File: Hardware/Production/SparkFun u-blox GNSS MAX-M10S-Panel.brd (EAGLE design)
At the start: 38.1 x 30.5 mm, 90 parts, among them J1 USB-to-Serial, J2 Qwiic RA, J3 PTH, J4 Qwiic RA, U1 MAX-M10S

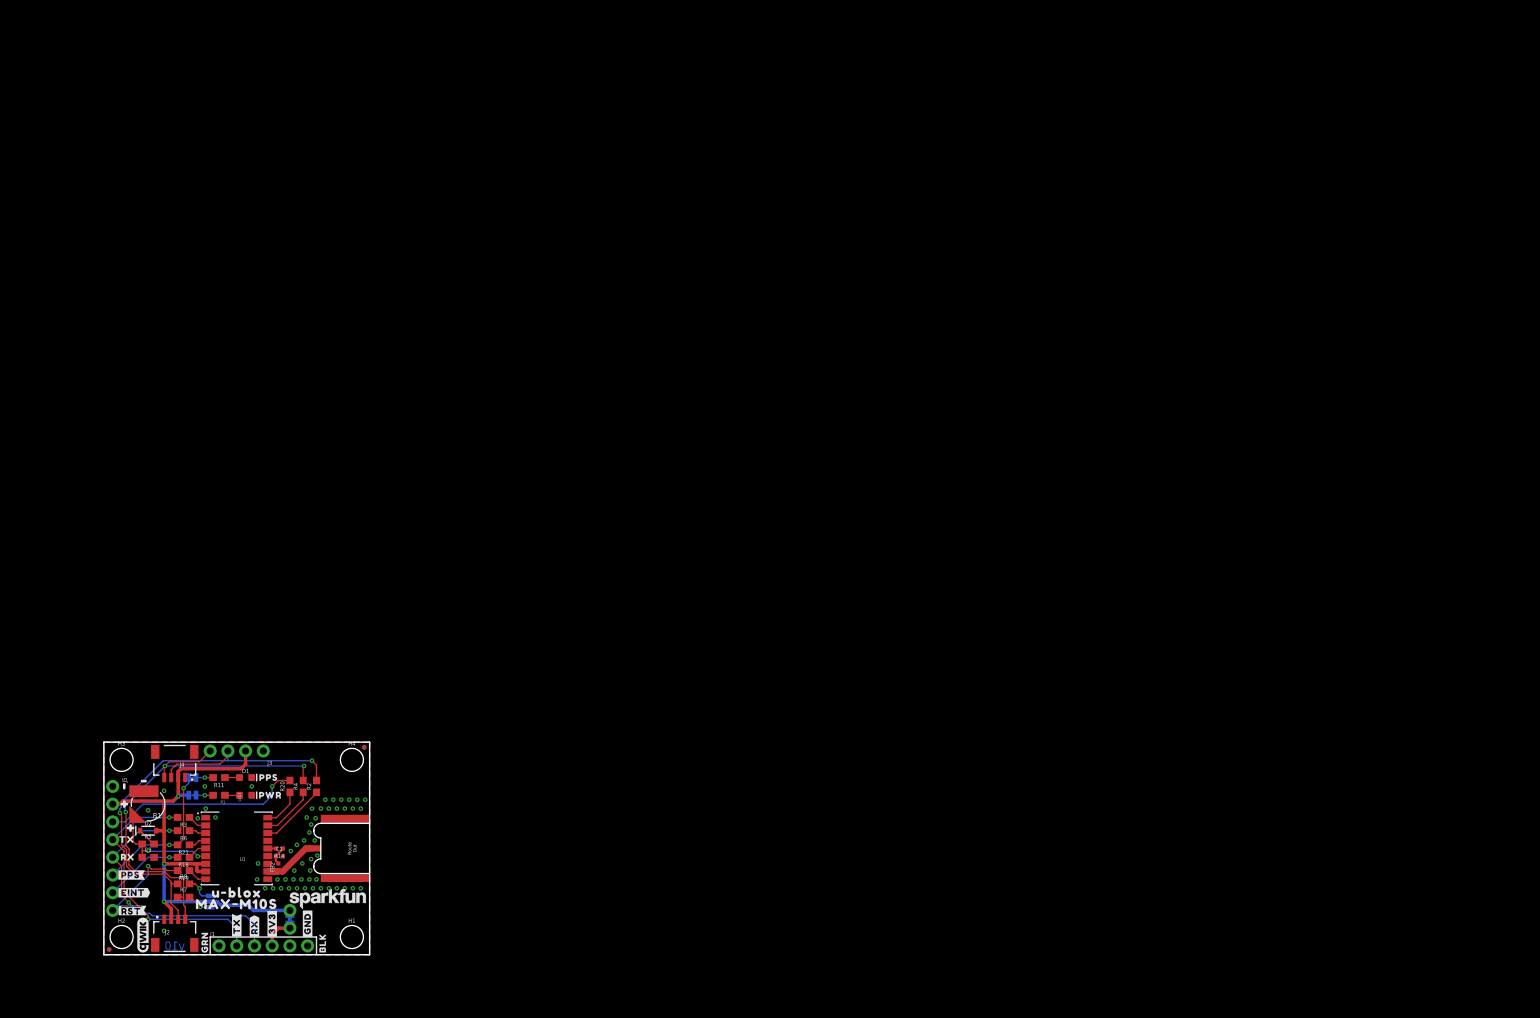
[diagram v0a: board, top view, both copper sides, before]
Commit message: Changing RF path to 0402. Adding GND vias on both RF trace sides. Adding panel.
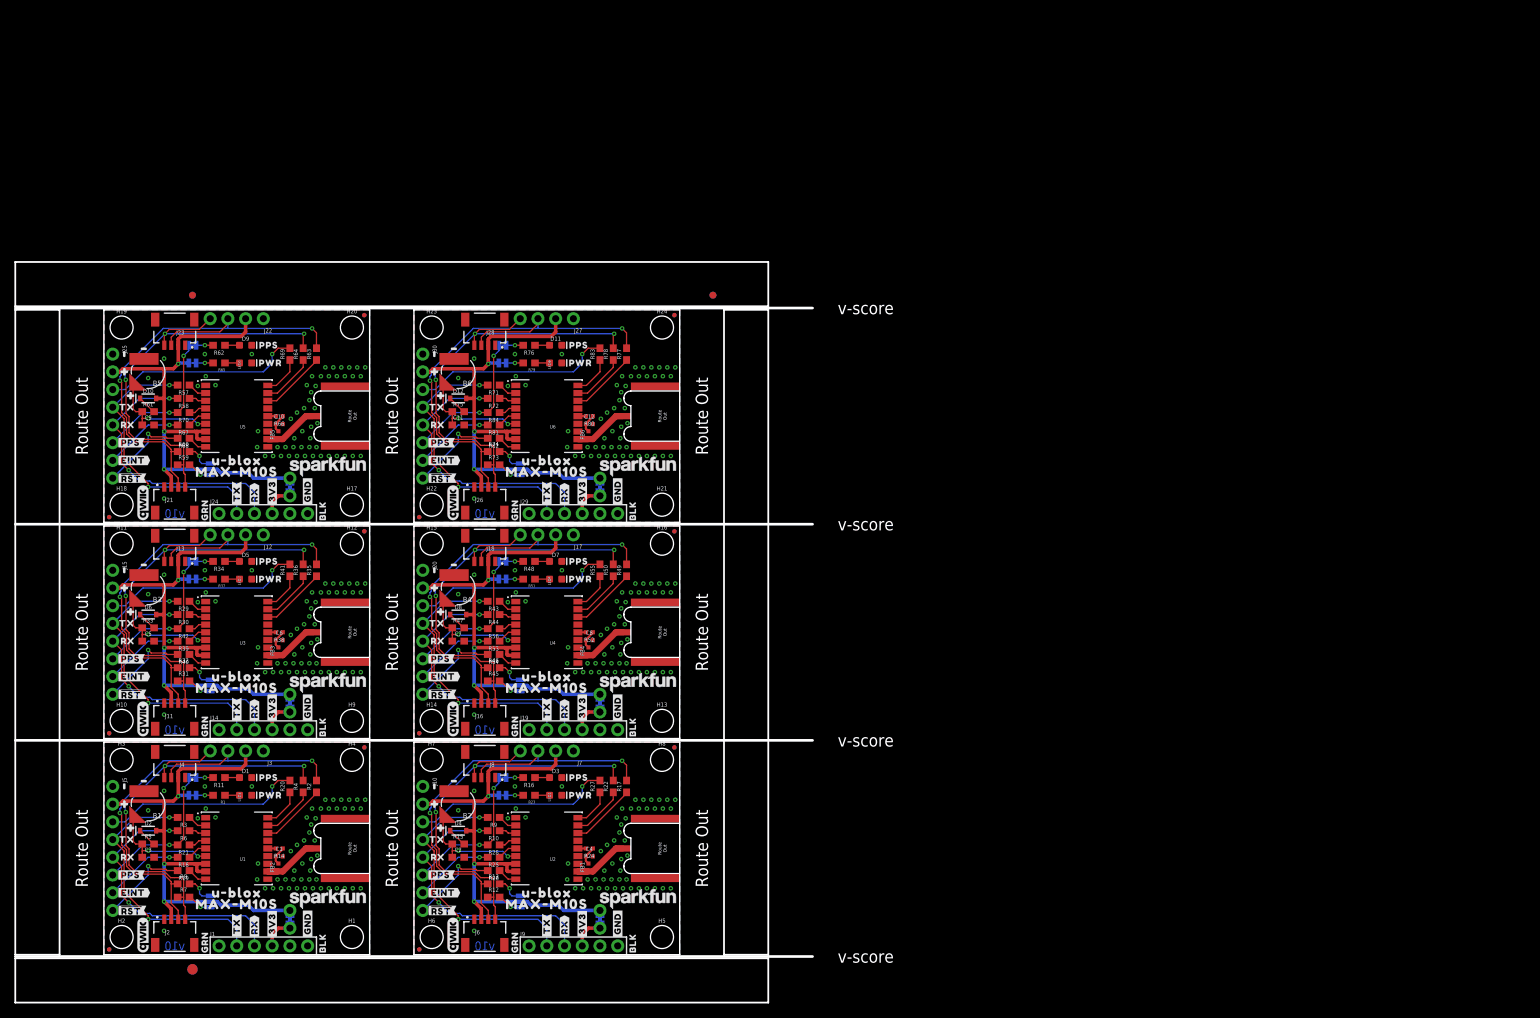
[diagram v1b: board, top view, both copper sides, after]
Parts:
- removed FRAME1: FRAME-LETTER, SparkFun-Aesthetics:CREATIVE_COMMONS
- added B2, B3, B4, B5, B6: 6.8MM_COIN_CELL, SparkFun-Batteries:ML414H_IV01E
- added C10, C12, C4, C6, C8: 47PF-0402_TIGHT-25V-5%-X7R, SparkFun-Capacitors:0402-TIGHT
- added C11, C2, C5, C7, C9: 1.0uF, SparkFun-Capacitors:0603
- added D10, D12, D4, D6, D8: 0.5A/40V/420mV, SparkFun-DiscreteSemi:SOD-323
- added D11, D3, D5, D7, D9: Yellow, SparkFun-LED:LED-0603
- added E$1, E$2, E$3, E$4: (no value), SparkFun-Aesthetics:FIDUCIAL-1X2
- added E$5, E$6: (no value), SparkFun-Retired:FIDUCIAL-1.5X3
- added E2, E3, E4, E5, E6: (no value), SparkFun-RF:SMA-EDGE-SMD
- added FB1, FB3, FB4, FB5, FB6: 2.66Ω, SparkFun-Coils:0402-TIGHT
- added FD10, FD11, FD12, FD13, FD14, FD15, FD16, FD17, FD18, FD19, FD20, FD21, FD22, FD23, FD24, FD5, FD6, FD7, FD8, FD9: FIDUCIALUFIDUCIAL, SparkFun-Aesthetics:FIDUCIAL-MICRO
- added H10, H11, H12, H13, H14, H15, H16, H17, H18, H19, H20, H21, H22, H23, H24, H5, H6, H7, H8, H9: STAND-OFF, SparkFun-Hardware:STAND-OFF
- added J10, J15, J20, J25, J30: (no value), SparkFun-Connectors:1X08_NO_SILK
- added J11, J13, J16, J18, J21, J23, J26, J28, J6, J8: Qwiic RA, SparkFun-Connectors:JST04_1MM_RA
- added J12, J17, J22, J27, J7: PTH, SparkX:1X04_NO_SILK
- added J14, J19, J24, J29, J9: USB-to-Serial, SparkFun-Connectors:1X06_NO_SILK
- added JP1, JP2, JP3, JP4, JP6: (no value), SparkFun-Jumpers:SMT-JUMPER_3_NO_SILK
- added LED1, LED3, LED4, LED5, LED6: RED, SparkFun-LED:LED-0603
- added LOGO10, LOGO14, LOGO18, LOGO22, LOGO6: SFE_LOGO_NAME_FLAME.1_INCH, SparkFun-Aesthetics:SFE_LOGO_NAME_FLAME_.1
- added LOGO11, LOGO15, LOGO19, LOGO23, LOGO7: QWIIC_LOGO_5MM, SparkFun-Aesthetics:QWIIC_5MM
- added LOGO12, LOGO16, LOGO20, LOGO24, LOGO8: SFE_LOGO_NAME.1_INCH, SparkFun-Aesthetics:SFE_LOGO_NAME_.1
- added LOGO13, LOGO17, LOGO21, LOGO5, LOGO9: OSHW-LOGOMINI, SparkFun-Aesthetics:OSHW-LOGO-MINI
- added MEAS1, MEAS2, MEAS3, MEAS4, MEAS5: (no value), SparkFun-Jumpers:COMBO-JUMPER_2_NC_TRACE
- added PPS_LED1, PPS_LED2, PPS_LED3, PPS_LED4, PPS_LED5, PWR1, PWR2, PWR3, PWR4, PWR5: (no value), SparkFun-Jumpers:SMT-JUMPER_2_NC_TRACE_SILK
- added R10, R17, R22, R25, R26, R27, R28, R29, R30, R35, R36, R39, R40, R41, R42, R43, R44, R49, R50, R53, R54, R55, R56, R57, R58, R63, R64, R67, R68, R69, R70, R71, R72, R77, R78, R81, R82, R83, R84, R9: 33, SparkFun-Resistors:0603
- added R12, R13, R31, R32, R45, R46, R59, R60, R73, R74: 2.2k, SparkFun-Resistors:0603
- added R15, R33, R47, R61, R75: 3.3k, SparkFun-Resistors:0603
- added R16, R23, R34, R37, R48, R51, R62, R65, R76, R79: 1k, SparkFun-Resistors:0603
- added R24, R38, R52, R66, R80: 33OHM-0402T-1/10W-1%, SparkFun-Resistors:0402-TIGHT
- added U$100, U$144, U$188, U$232, U$56: (no value), output:##SAFE##0
- added U$101, U$126, U$145, U$170, U$189, U$214, U$233, U$258, U$57, U$82: (no value), output:#PPS#1
- added U$102, U$146, U$190, U$234, U$58: (no value), output:#RX#1
- added U$103, U$147, U$191, U$235, U$59: (no value), output:#TX#0
- added U$104, U$107, U$148, U$151, U$192, U$195, U$236, U$239, U$60, U$63: (no value), output:MAX#M10S1
- added U$105, U$106, U$149, U$150, U$193, U$194, U$237, U$238, U$61, U$62: (no value), output:U#BLOX0
- added U$108, U$152, U$196, U$240, U$64: (no value), output:SMA2
- added U$109, U$140, U$153, U$184, U$197, U$228, U$241, U$52, U$65, U$96: (no value), output:#TX#3
- added U$110, U$139, U$154, U$183, U$198, U$227, U$242, U$51, U$66, U$95: (no value), output:#RX#2
- added U$111, U$118, U$133, U$141, U$155, U$162, U$177, U$185, U$199, U$206, U$221, U$229, U$243, U$250, U$53, U$67, U$74, U$89, U$97: (no value), output:#3V3#4
- added U$112, U$119, U$134, U$142, U$156, U$163, U$17, U$178, U$186, U$200, U$207, U$222, U$230, U$244, U$251, U$54, U$68, U$75, U$90, U$98: (no value), output:#GND#5
- added U$113, U$135, U$157, U$179, U$201, U$223, U$245, U$47, U$69, U$91: (no value), output:BLK0
- added U$114, U$136, U$158, U$180, U$202, U$224, U$246, U$48, U$70, U$92: (no value), output:GRN1
- added U$115, U$159, U$203, U$247, U$71: (no value), output:#I�C#0
- added U$116, U$160, U$204, U$248, U$72: (no value), output:#SCL#1
- added U$117, U$161, U$205, U$249, U$73: (no value), output:#SDA#0
- added U$120, U$164, U$208, U$252, U$76: (no value), output:#PPS#0
- added U$121, U$165, U$209, U$253, U$77: (no value), output:#PWR#0
- added U$122, U$129, U$166, U$173, U$210, U$217, U$254, U$261, U$78, U$85: (no value), output:#0
- added U$123, U$130, U$167, U$174, U$211, U$218, U$255, U$262, U$79, U$86: (no value), output:#1
- added U$124, U$168, U$212, U$256, U$80: (no value), output:##RST##0
- added U$125, U$169, U$213, U$257, U$81: (no value), output:#EINT#0
- added U$127, U$171, U$215, U$259, U$83: (no value), output:RX2
- added U$128, U$172, U$216, U$260, U$84: (no value), output:TX3
- added U$131, U$175, U$219, U$263, U$87: (no value), output:#MEAS#0
- added U$132, U$176, U$220, U$264, U$88: (no value), output:#EINT_#0
- added U$137, U$181, U$225, U$49, U$93: (no value), output:PPS7
- added U$138, U$182, U$226, U$50, U$94: (no value), output:PWR6
- added U$143, U$187, U$231, U$55, U$99: (no value), output:##RST##2
- added U2, U3, U4, U5, U6: MAX-M10S, GNSS-MAX:MAX-M10S
- U$2: value SPECIAL_INSTRUCTIONS-ORDERING -> (none); device SparkFun-Aesthetics:ORDERING_INSTRUCTIONS -> output:#3V3#4
- moved U$2 51.5 mm to (68.6, 4.45), turned to 90 degrees
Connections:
- new net !RESET1: J10.8, R26.2
- new net !RESET2: J15.8, R40.2
- new net !RESET3: J20.8, R54.2
- new net !RESET4: J25.8, R68.2
- new net !RESET5: J30.8, R82.2
- new net !SAFE1: J10.3, R27.2
- new net !SAFE2: J15.3, R41.2
- new net !SAFE3: J20.3, R55.2
- new net !SAFE4: J25.3, R69.2
- new net !SAFE5: J30.3, R83.2
- new net 3.3V1: D4.A, J10.2, J6.2, J7.2, J8.2, JP1.2, MEAS1.2, MEAS1.4, PWR1.2, U2.7, U2.8
- new net 3.3V2: D6.A, J11.2, J12.2, J13.2, J15.2, JP2.2, MEAS2.2, MEAS2.4, PWR2.2, U3.7, U3.8
- new net 3.3V3: D8.A, J16.2, J17.2, J18.2, J20.2, JP3.2, MEAS3.2, MEAS3.4, PWR3.2, U4.7, U4.8
- new net 3.3V4: D10.A, J21.2, J22.2, J23.2, J25.2, JP4.2, MEAS4.2, MEAS4.4, PWR4.2, U5.7, U5.8
- new net 3.3V5: D12.A, J26.2, J27.2, J28.2, J30.2, JP6.2, MEAS5.2, MEAS5.4, PWR5.2, U6.7, U6.8
- new net ANT_VCC1: C4.1, FB1.2, R24.1
- new net ANT_VCC2: C6.1, FB3.2, R38.1
- new net ANT_VCC3: C8.1, FB4.2, R52.1
- new net ANT_VCC4: C10.1, FB5.2, R66.1
- new net ANT_VCC5: C12.1, FB6.2, R80.1
- new net BACKUP1: B2.+, C2.1, R15.1, U2.6
- new net BACKUP2: B3.+, C5.1, R33.1, U3.6
- new net BACKUP3: B4.+, C7.1, R47.1, U4.6
- new net BACKUP4: B5.+, C9.1, R61.1, U5.6
- new net BACKUP5: B6.+, C11.1, R75.1, U6.6
- new net EXTINT_LV1: R25.1, U2.5
- new net EXTINT_LV2: R39.1, U3.5
- new net EXTINT_LV3: R53.1, U4.5
- new net EXTINT_LV4: R67.1, U5.5
- new net EXTINT_LV5: R81.1, U6.5
- new net GND1: B2.-, C2.2, C4.2, D3.C, E2.GND@0, E2.GND@1, J10.1, J6.1, J7.1, J8.1, J9.6, LED1.C, U2.1, U2.10, U2.12
- new net GND2: B3.-, C5.2, C6.2, D5.C, E3.GND@0, E3.GND@1, J11.1, J12.1, J13.1, J14.6, J15.1, LED3.C, U3.1, U3.10, U3.12
- new net GND3: B4.-, C7.2, C8.2, D7.C, E4.GND@0, E4.GND@1, J16.1, J17.1, J18.1, J19.6, J20.1, LED4.C, U4.1, U4.10, U4.12
- new net GND4: B5.-, C10.2, C9.2, D9.C, E5.GND@0, E5.GND@1, J21.1, J22.1, J23.1, J24.6, J25.1, LED5.C, U5.1, U5.10, U5.12
- new net GND5: B6.-, C11.2, C12.2, D11.C, E6.GND@0, E6.GND@1, J26.1, J27.1, J28.1, J29.6, J30.1, LED6.C, U6.1, U6.10, U6.12
- new net GPS_RF1: E2.SIG, FB1.1, U2.11
- new net GPS_RF2: E3.SIG, FB3.1, U3.11
- new net GPS_RF3: E4.SIG, FB4.1, U4.11
- new net GPS_RF4: E5.SIG, FB5.1, U5.11
- new net GPS_RF5: E6.SIG, FB6.1, U6.11
- new net INT1: J10.7, R25.2
- new net INT2: J15.7, R39.2
- new net INT3: J20.7, R53.2
- new net INT4: J25.7, R67.2
- new net INT5: J30.7, R81.2
- new net N$11: PPS_LED1.1, R16.2
- new net N$12: D4.C, R15.2
- new net N$13: LED1.A, R23.1
- new net N$14: PWR1.1, R23.2
- new net N$15: J9.4, MEAS1.1, MEAS1.3
- new net N$16: JP2.1, R32.2
- new net N$18: JP2.3, R31.2
- new net N$19: D5.A, R34.1
- new net N$20: PPS_LED2.1, R34.2
- new net N$21: D6.C, R33.2
- new net N$22: LED3.A, R37.1
- new net N$23: PWR2.1, R37.2
- new net N$24: J14.4, MEAS2.1, MEAS2.3
- new net N$25: JP3.1, R46.2
- new net N$26: JP3.3, R45.2
- new net N$27: D7.A, R48.1
- new net N$28: PPS_LED3.1, R48.2
- new net N$29: D8.C, R47.2
- new net N$3: JP1.1, R13.2
- new net N$30: LED4.A, R51.1
- new net N$31: PWR3.1, R51.2
- new net N$32: J19.4, MEAS3.1, MEAS3.3
- new net N$33: JP4.1, R60.2
- new net N$34: JP4.3, R59.2
- new net N$35: D9.A, R62.1
- new net N$36: PPS_LED4.1, R62.2
- new net N$37: D10.C, R61.2
- new net N$38: LED5.A, R65.1
- new net N$39: PWR4.1, R65.2
- new net N$40: J24.4, MEAS4.1, MEAS4.3
- new net N$41: JP6.1, R74.2
- new net N$42: JP6.3, R73.2
- new net N$43: D11.A, R76.1
- new net N$44: PPS_LED5.1, R76.2
- new net N$45: D12.C, R75.2
- new net N$46: LED6.A, R79.1
- new net N$47: PWR5.1, R79.2
- new net N$48: J29.4, MEAS5.1, MEAS5.3
- new net N$7: JP1.3, R12.2
- new net N$9: D3.A, R16.1
- new net PPS1: J10.6, PPS_LED1.2, R28.2
- new net PPS2: J15.6, PPS_LED2.2, R42.2
- new net PPS3: J20.6, PPS_LED3.2, R56.2
- new net PPS4: J25.6, PPS_LED4.2, R70.2
- new net PPS5: J30.6, PPS_LED5.2, R84.2
- new net PPS_LV1: R28.1, U2.4
- new net PPS_LV2: R42.1, U3.4
- new net PPS_LV3: R56.1, U4.4
- new net PPS_LV4: R70.1, U5.4
- new net PPS_LV5: R84.1, U6.4
- new net RST_LV1: R26.1, U2.9
- new net RST_LV2: R40.1, U3.9
- new net RST_LV3: R54.1, U4.9
- new net RST_LV4: R68.1, U5.9
- new net RST_LV5: R82.1, U6.9
- new net RXI1: J10.5, J9.3, R10.2
- new net RXI2: J14.3, J15.5, R30.2
- new net RXI3: J19.3, J20.5, R44.2
- new net RXI4: J24.3, J25.5, R58.2
- new net RXI5: J29.3, J30.5, R72.2
- new net RXLV1: R10.1, U2.3
- new net RXLV2: R30.1, U3.3
- new net RXLV3: R44.1, U4.3
- new net RXLV4: R58.1, U5.3
- new net RXLV5: R72.1, U6.3
- new net SAFE_LV1: R27.1, U2.18
- new net SAFE_LV2: R41.1, U3.18
- new net SAFE_LV3: R55.1, U4.18
- new net SAFE_LV4: R69.1, U5.18
- new net SAFE_LV5: R83.1, U6.18
- new net SCL1: J6.4, J7.4, J8.4, R12.1, R22.2
- new net SCL2: J11.4, J12.4, J13.4, R31.1, R36.2
- new net SCL3: J16.4, J17.4, J18.4, R45.1, R50.2
- new net SCL4: J21.4, J22.4, J23.4, R59.1, R64.2
- new net SCL5: J26.4, J27.4, J28.4, R73.1, R78.2
- new net SCL_LV1: R22.1, U2.17
- new net SCL_LV2: R36.1, U3.17
- new net SCL_LV3: R50.1, U4.17
- new net SCL_LV4: R64.1, U5.17
- new net SCL_LV5: R78.1, U6.17
- new net SDA1: J6.3, J7.3, J8.3, R13.1, R17.2
- new net SDA2: J11.3, J12.3, J13.3, R32.1, R35.2
- new net SDA3: J16.3, J17.3, J18.3, R46.1, R49.2
- new net SDA4: J21.3, J22.3, J23.3, R60.1, R63.2
- new net SDA5: J26.3, J27.3, J28.3, R74.1, R77.2
- new net SDA_LV1: R17.1, U2.16
- new net SDA_LV2: R35.1, U3.16
- new net SDA_LV3: R49.1, U4.16
- new net SDA_LV4: R63.1, U5.16
- new net SDA_LV5: R77.1, U6.16
- new net TXLV1: R9.1, U2.2
- new net TXLV2: R29.1, U3.2
- new net TXLV3: R43.1, U4.2
- new net TXLV4: R57.1, U5.2
- new net TXLV5: R71.1, U6.2
- new net TXO1: J10.4, J9.2, R9.2
- new net TXO2: J14.2, J15.4, R29.2
- new net TXO3: J19.2, J20.4, R43.2
- new net TXO4: J24.2, J25.4, R57.2
- new net TXO5: J29.2, J30.4, R71.2
- new net VCC_RF1: R24.2, U2.14
- new net VCC_RF2: R38.2, U3.14
- new net VCC_RF3: R52.2, U4.14
- new net VCC_RF4: R66.2, U5.14
- new net VCC_RF5: R80.2, U6.14
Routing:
- net 3.3V5: track 0.00 -> 73.1 mm, vias 0 -> 3
- net 3.3V4: track 0.00 -> 73.1 mm, vias 0 -> 3
- net 3.3V1: track 0.00 -> 73.1 mm, vias 0 -> 3
- net 3.3V3: track 0.00 -> 73.1 mm, vias 0 -> 3
- net 3.3V2: track 0.00 -> 73.1 mm, vias 0 -> 3
- net SDA4: track 0.00 -> 68.8 mm, vias 0 -> 2
- net SDA5: track 0.00 -> 68.8 mm, vias 0 -> 2
- net SDA3: track 0.00 -> 68.8 mm, vias 0 -> 2
- net SDA2: track 0.00 -> 68.8 mm, vias 0 -> 2
- net SDA1: track 0.00 -> 68.8 mm, vias 0 -> 2
- net SCL5: track 0.00 -> 63.3 mm, vias 0 -> 3
- net SCL4: track 0.00 -> 63.3 mm, vias 0 -> 3
- net SCL3: track 0.00 -> 63.3 mm, vias 0 -> 3
- net SCL1: track 0.00 -> 63.3 mm, vias 0 -> 3
- net SCL2: track 0.00 -> 63.3 mm, vias 0 -> 3
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- added copper zone on layer 1, net GND1
- added copper zone on layer 16, net GND1
- added copper zone on layer 1, net GND2
- added copper zone on layer 16, net GND2
- added copper zone on layer 1, net GND3
- added copper zone on layer 16, net GND3
- added copper zone on layer 1, net GND4
- added copper zone on layer 16, net GND4
- added copper zone on layer 1, net GND5
- added copper zone on layer 16, net GND5
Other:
- board size 38.1 x 30.5 mm -> 114.3 x 106.2 mm
- board text added: "Route Out"
- board text added: "v-score"
- board text removed: "2 Layer Board"
- board text removed: "Board thickness is 1.6mm"
- board text removed: "Measurements in inches"
- board text removed: "N. Seidle"

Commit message: Add ESD RF diode. Change to PTH SMA.
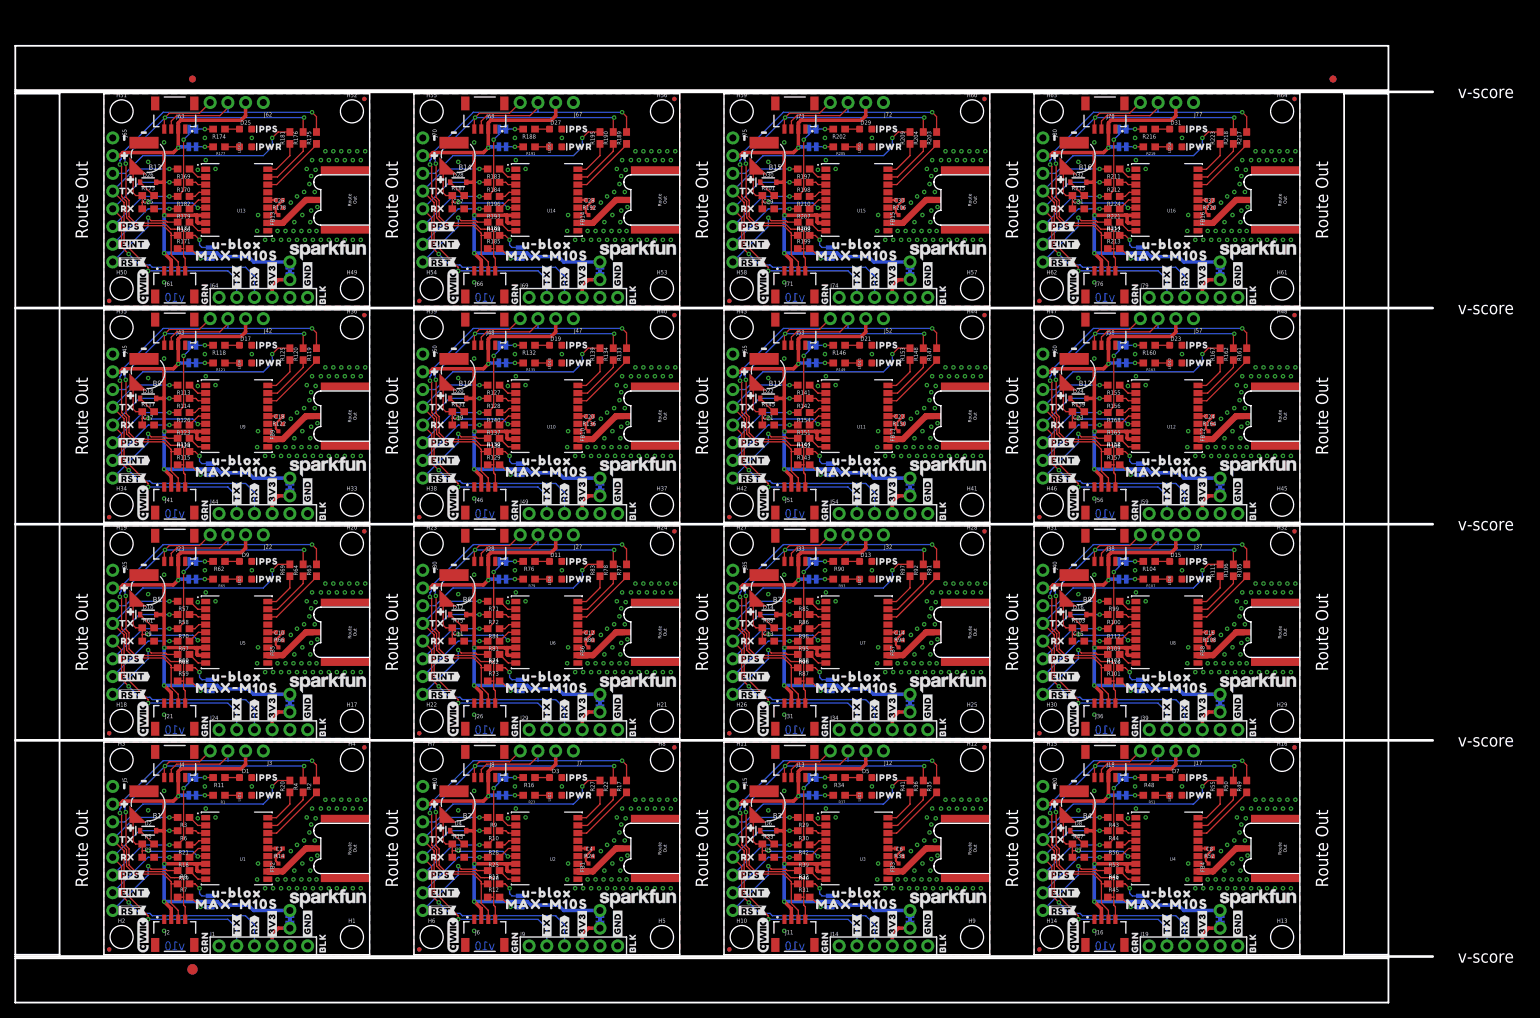
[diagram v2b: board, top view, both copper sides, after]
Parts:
- added B10, B11, B12, B13, B14, B15, B16, B7, B8, B9: 6.8MM_COIN_CELL, SparkFun-Batteries:ML414H_IV01E
- added C13, C15, C17, C19, C21, C23, C25, C27, C29, C31: 1.0uF, SparkFun-Capacitors:0603
- added C14, C16, C18, C20, C22, C24, C26, C28, C30, C32: 47PF-0402_TIGHT-25V-5%-X7R, SparkFun-Capacitors:0402-TIGHT
- added D13, D15, D17, D19, D21, D23, D25, D27, D29, D31: Yellow, SparkFun-LED:LED-0603
- added D14, D16, D18, D20, D22, D24, D26, D28, D30, D32: 0.5A/40V/420mV, SparkFun-DiscreteSemi:SOD-323
- added E10, E11, E12, E13, E14, E15, E16, E7, E8, E9: (no value), SparkFun-RF:SMA-EDGE-SMD
- added FB10, FB11, FB12, FB13, FB14, FB15, FB16, FB7, FB8, FB9: 2.66Ω, SparkFun-Coils:0402-TIGHT
- added FD25, FD26, FD27, FD28, FD29, FD30, FD31, FD32, FD33, FD34, FD35, FD36, FD37, FD38, FD39, FD40, FD41, FD42, FD43, FD44, FD45, FD46, FD47, FD48, FD49, FD50, FD51, FD52, FD53, FD54, FD55, FD56, FD57, FD58, FD59, FD60, FD61, FD62, FD63, FD64: FIDUCIALUFIDUCIAL, SparkFun-Aesthetics:FIDUCIAL-MICRO
- added H25, H26, H27, H28, H29, H30, H31, H32, H33, H34, H35, H36, H37, H38, H39, H40, H41, H42, H43, H44, H45, H46, H47, H48, H49, H50, H51, H52, H53, H54, H55, H56, H57, H58, H59, H60, H61, H62, H63, H64: STAND-OFF, SparkFun-Hardware:STAND-OFF
- added J31, J33, J36, J38, J41, J43, J46, J48, J51, J53, J56, J58, J61, J63, J66, J68, J71, J73, J76, J78: Qwiic RA, SparkFun-Connectors:JST04_1MM_RA
- added J32, J37, J42, J47, J52, J57, J62, J67, J72, J77: PTH, SparkX:1X04_NO_SILK
- added J34, J39, J44, J49, J54, J59, J64, J69, J74, J79: USB-to-Serial, SparkFun-Connectors:1X06_NO_SILK
- added J35, J40, J45, J50, J55, J60, J65, J70, J75, J80: (no value), SparkFun-Connectors:1X08_NO_SILK
- added JP10, JP11, JP12, JP13, JP14, JP15, JP16, JP7, JP8, JP9: (no value), SparkFun-Jumpers:SMT-JUMPER_3_NO_SILK
- added LED10, LED11, LED12, LED13, LED14, LED15, LED16, LED7, LED8, LED9: RED, SparkFun-LED:LED-0603
- added LOGO25, LOGO29, LOGO33, LOGO37, LOGO41, LOGO45, LOGO49, LOGO53, LOGO57, LOGO61: OSHW-LOGOMINI, SparkFun-Aesthetics:OSHW-LOGO-MINI
- added LOGO26, LOGO30, LOGO34, LOGO38, LOGO42, LOGO46, LOGO50, LOGO54, LOGO58, LOGO62: SFE_LOGO_NAME_FLAME.1_INCH, SparkFun-Aesthetics:SFE_LOGO_NAME_FLAME_.1
- added LOGO27, LOGO31, LOGO35, LOGO39, LOGO43, LOGO47, LOGO51, LOGO55, LOGO59, LOGO63: QWIIC_LOGO_5MM, SparkFun-Aesthetics:QWIIC_5MM
- added LOGO28, LOGO32, LOGO36, LOGO40, LOGO44, LOGO48, LOGO52, LOGO56, LOGO60, LOGO64: SFE_LOGO_NAME.1_INCH, SparkFun-Aesthetics:SFE_LOGO_NAME_.1
- added MEAS10, MEAS11, MEAS12, MEAS13, MEAS14, MEAS15, MEAS6, MEAS7, MEAS8, MEAS9: (no value), SparkFun-Jumpers:COMBO-JUMPER_2_NC_TRACE
- added PPS_LED10, PPS_LED11, PPS_LED12, PPS_LED13, PPS_LED14, PPS_LED15, PPS_LED6, PPS_LED7, PPS_LED8, PPS_LED9, PWR10, PWR11, PWR12, PWR13, PWR14, PWR15, PWR6, PWR7, PWR8, PWR9: (no value), SparkFun-Jumpers:SMT-JUMPER_2_NC_TRACE_SILK
- added R100, R105, R106, R109, R110, R111, R112, R113, R114, R119, R120, R123, R124, R125, R126, R127, R128, R133, R134, R137, R138, R139, R140, R141, R142, R147, R148, R151, R152, R153, R154, R155, R156, R161, R162, R165, R166, R167, R168, R169, R170, R175, R176, R179, R180, R181, R182, R183, R184, R189, R190, R193, R194, R195, R196, R197, R198, R203, R204, R207, R208, R209, R210, R211, R212, R217, R218, R221, R222, R223, R224, R85, R86, R91, R92, R95, R96, R97, R98, R99: 33, SparkFun-Resistors:0603
- added R101, R102, R115, R116, R129, R130, R143, R144, R157, R158, R171, R172, R185, R186, R199, R200, R213, R214, R87, R88: 2.2k, SparkFun-Resistors:0603
- added R103, R117, R131, R145, R159, R173, R187, R201, R215, R89: 3.3k, SparkFun-Resistors:0603
- added R104, R107, R118, R121, R132, R135, R146, R149, R160, R163, R174, R177, R188, R191, R202, R205, R216, R219, R90, R93: 1k, SparkFun-Resistors:0603
- added R108, R122, R136, R150, R164, R178, R192, R206, R220, R94: 33OHM-0402T-1/10W-1%, SparkFun-Resistors:0402-TIGHT
- added U$265, U$273, U$287, U$294, U$309, U$317, U$331, U$338, U$353, U$361, U$375, U$382, U$397, U$405, U$419, U$426, U$441, U$449, U$463, U$470, U$485, U$493, U$507, U$514, U$529, U$537, U$551, U$558, U$573, U$581, U$595, U$602, U$617, U$625, U$639, U$646, U$661, U$669, U$683, U$690: (no value), output:#3V3#4
- added U$266, U$274, U$288, U$295, U$310, U$318, U$332, U$339, U$354, U$362, U$376, U$383, U$398, U$406, U$420, U$427, U$442, U$450, U$464, U$471, U$486, U$494, U$508, U$515, U$530, U$538, U$552, U$559, U$574, U$582, U$596, U$603, U$618, U$626, U$640, U$647, U$662, U$670, U$684, U$691: (no value), output:#GND#5
- added U$267, U$289, U$311, U$333, U$355, U$377, U$399, U$421, U$443, U$465, U$487, U$509, U$531, U$553, U$575, U$597, U$619, U$641, U$663, U$685: (no value), output:BLK0
- added U$268, U$290, U$312, U$334, U$356, U$378, U$400, U$422, U$444, U$466, U$488, U$510, U$532, U$554, U$576, U$598, U$620, U$642, U$664, U$686: (no value), output:GRN1
- added U$269, U$313, U$357, U$401, U$445, U$489, U$533, U$577, U$621, U$665: (no value), output:PPS7
- added U$270, U$314, U$358, U$402, U$446, U$490, U$534, U$578, U$622, U$666: (no value), output:PWR6
- added U$271, U$286, U$315, U$330, U$359, U$374, U$403, U$418, U$447, U$462, U$491, U$506, U$535, U$550, U$579, U$594, U$623, U$638, U$667, U$682: (no value), output:#RX#2
- added U$272, U$285, U$316, U$329, U$360, U$373, U$404, U$417, U$448, U$461, U$492, U$505, U$536, U$549, U$580, U$593, U$624, U$637, U$668, U$681: (no value), output:#TX#3
- added U$275, U$319, U$363, U$407, U$451, U$495, U$539, U$583, U$627, U$671: (no value), output:##RST##2
- added U$276, U$320, U$364, U$408, U$452, U$496, U$540, U$584, U$628, U$672: (no value), output:##SAFE##0
- added U$277, U$302, U$321, U$346, U$365, U$390, U$409, U$434, U$453, U$478, U$497, U$522, U$541, U$566, U$585, U$610, U$629, U$654, U$673, U$698: (no value), output:#PPS#1
- added U$278, U$322, U$366, U$410, U$454, U$498, U$542, U$586, U$630, U$674: (no value), output:#RX#1
- added U$279, U$323, U$367, U$411, U$455, U$499, U$543, U$587, U$631, U$675: (no value), output:#TX#0
- added U$280, U$283, U$324, U$327, U$368, U$371, U$412, U$415, U$456, U$459, U$500, U$503, U$544, U$547, U$588, U$591, U$632, U$635, U$676, U$679: (no value), output:MAX#M10S1
- added U$281, U$282, U$325, U$326, U$369, U$370, U$413, U$414, U$457, U$458, U$501, U$502, U$545, U$546, U$589, U$590, U$633, U$634, U$677, U$678: (no value), output:U#BLOX0
- added U$284, U$328, U$372, U$416, U$460, U$504, U$548, U$592, U$636, U$680: (no value), output:SMA2
- added U$291, U$335, U$379, U$423, U$467, U$511, U$555, U$599, U$643, U$687: (no value), output:#I�C#0
- added U$292, U$336, U$380, U$424, U$468, U$512, U$556, U$600, U$644, U$688: (no value), output:#SCL#1
- added U$293, U$337, U$381, U$425, U$469, U$513, U$557, U$601, U$645, U$689: (no value), output:#SDA#0
- added U$296, U$340, U$384, U$428, U$472, U$516, U$560, U$604, U$648, U$692: (no value), output:#PPS#0
- added U$297, U$341, U$385, U$429, U$473, U$517, U$561, U$605, U$649, U$693: (no value), output:#PWR#0
- added U$298, U$305, U$342, U$349, U$386, U$393, U$430, U$437, U$474, U$481, U$518, U$525, U$562, U$569, U$606, U$613, U$650, U$657, U$694, U$701: (no value), output:#0
- added U$299, U$306, U$343, U$350, U$387, U$394, U$431, U$438, U$475, U$482, U$519, U$526, U$563, U$570, U$607, U$614, U$651, U$658, U$695, U$702: (no value), output:#1
- added U$300, U$344, U$388, U$432, U$476, U$520, U$564, U$608, U$652, U$696: (no value), output:##RST##0
- added U$301, U$345, U$389, U$433, U$477, U$521, U$565, U$609, U$653, U$697: (no value), output:#EINT#0
- added U$303, U$347, U$391, U$435, U$479, U$523, U$567, U$611, U$655, U$699: (no value), output:RX2
- added U$304, U$348, U$392, U$436, U$480, U$524, U$568, U$612, U$656, U$700: (no value), output:TX3
- added U$307, U$351, U$395, U$439, U$483, U$527, U$571, U$615, U$659, U$703: (no value), output:#MEAS#0
- added U$308, U$352, U$396, U$440, U$484, U$528, U$572, U$616, U$660, U$704: (no value), output:#EINT_#0
- added U10, U11, U12, U13, U14, U15, U16, U7, U8, U9: MAX-M10S, GNSS-MAX:MAX-M10S
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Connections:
- new net !RESET10: J55.8, R152.2
- new net !RESET11: J60.8, R166.2
- new net !RESET12: J65.8, R180.2
- new net !RESET13: J70.8, R194.2
- new net !RESET14: J75.8, R208.2
- new net !RESET15: J80.8, R222.2
- new net !RESET6: J35.8, R96.2
- new net !RESET7: J40.8, R110.2
- new net !RESET8: J45.8, R124.2
- new net !RESET9: J50.8, R138.2
- new net !SAFE10: J55.3, R153.2
- new net !SAFE11: J60.3, R167.2
- new net !SAFE12: J65.3, R181.2
- new net !SAFE13: J70.3, R195.2
- new net !SAFE14: J75.3, R209.2
- new net !SAFE15: J80.3, R223.2
- new net !SAFE6: J35.3, R97.2
- new net !SAFE7: J40.3, R111.2
- new net !SAFE8: J45.3, R125.2
- new net !SAFE9: J50.3, R139.2
- new net 3.3V10: D22.A, J51.2, J52.2, J53.2, J55.2, JP11.2, MEAS10.2, MEAS10.4, PWR10.2, U11.7, U11.8
- new net 3.3V11: D24.A, J56.2, J57.2, J58.2, J60.2, JP12.2, MEAS11.2, MEAS11.4, PWR11.2, U12.7, U12.8
- new net 3.3V12: D26.A, J61.2, J62.2, J63.2, J65.2, JP13.2, MEAS12.2, MEAS12.4, PWR12.2, U13.7, U13.8
- new net 3.3V13: D28.A, J66.2, J67.2, J68.2, J70.2, JP14.2, MEAS13.2, MEAS13.4, PWR13.2, U14.7, U14.8
- new net 3.3V14: D30.A, J71.2, J72.2, J73.2, J75.2, JP15.2, MEAS14.2, MEAS14.4, PWR14.2, U15.7, U15.8
- new net 3.3V15: D32.A, J76.2, J77.2, J78.2, J80.2, JP16.2, MEAS15.2, MEAS15.4, PWR15.2, U16.7, U16.8
- new net 3.3V6: D14.A, J31.2, J32.2, J33.2, J35.2, JP7.2, MEAS6.2, MEAS6.4, PWR6.2, U7.7, U7.8
- new net 3.3V7: D16.A, J36.2, J37.2, J38.2, J40.2, JP8.2, MEAS7.2, MEAS7.4, PWR7.2, U8.7, U8.8
- new net 3.3V8: D18.A, J41.2, J42.2, J43.2, J45.2, JP9.2, MEAS8.2, MEAS8.4, PWR8.2, U9.7, U9.8
- new net 3.3V9: D20.A, J46.2, J47.2, J48.2, J50.2, JP10.2, MEAS9.2, MEAS9.4, PWR9.2, U10.7, U10.8
- new net ANT_VCC10: C22.1, FB11.2, R150.1
- new net ANT_VCC11: C24.1, FB12.2, R164.1
- new net ANT_VCC12: C26.1, FB13.2, R178.1
- new net ANT_VCC13: C28.1, FB14.2, R192.1
- new net ANT_VCC14: C30.1, FB15.2, R206.1
- new net ANT_VCC15: C32.1, FB16.2, R220.1
- new net ANT_VCC6: C14.1, FB7.2, R94.1
- new net ANT_VCC7: C16.1, FB8.2, R108.1
- new net ANT_VCC8: C18.1, FB9.2, R122.1
- new net ANT_VCC9: C20.1, FB10.2, R136.1
- new net BACKUP10: B11.+, C21.1, R145.1, U11.6
- new net BACKUP11: B12.+, C23.1, R159.1, U12.6
- new net BACKUP12: B13.+, C25.1, R173.1, U13.6
- new net BACKUP13: B14.+, C27.1, R187.1, U14.6
- new net BACKUP14: B15.+, C29.1, R201.1, U15.6
- new net BACKUP15: B16.+, C31.1, R215.1, U16.6
- new net BACKUP6: B7.+, C13.1, R89.1, U7.6
- new net BACKUP7: B8.+, C15.1, R103.1, U8.6
- new net BACKUP8: B9.+, C17.1, R117.1, U9.6
- new net BACKUP9: B10.+, C19.1, R131.1, U10.6
- new net EXTINT_LV10: R151.1, U11.5
- new net EXTINT_LV11: R165.1, U12.5
- new net EXTINT_LV12: R179.1, U13.5
- new net EXTINT_LV13: R193.1, U14.5
- new net EXTINT_LV14: R207.1, U15.5
- new net EXTINT_LV15: R221.1, U16.5
- new net EXTINT_LV6: R95.1, U7.5
- new net EXTINT_LV7: R109.1, U8.5
- new net EXTINT_LV8: R123.1, U9.5
- new net EXTINT_LV9: R137.1, U10.5
- new net GND10: B11.-, C21.2, C22.2, D21.C, E11.GND@0, E11.GND@1, J51.1, J52.1, J53.1, J54.6, J55.1, LED11.C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
- new net GND11: B12.-, C23.2, C24.2, D23.C, E12.GND@0, E12.GND@1, J56.1, J57.1, J58.1, J59.6, J60.1, LED12.C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
- new net GND12: B13.-, C25.2, C26.2, D25.C, E13.GND@0, E13.GND@1, J61.1, J62.1, J63.1, J64.6, J65.1, LED13.C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
- new net GND13: B14.-, C27.2, C28.2, D27.C, E14.GND@0, E14.GND@1, J66.1, J67.1, J68.1, J69.6, J70.1, LED14.C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
- new net GND14: B15.-, C29.2, C30.2, D29.C, E15.GND@0, E15.GND@1, J71.1, J72.1, J73.1, J74.6, J75.1, LED15.C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
- new net GND15: B16.-, C31.2, C32.2, D31.C, E16.GND@0, E16.GND@1, J76.1, J77.1, J78.1, J79.6, J80.1, LED16.C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
- new net GND6: B7.-, C13.2, C14.2, D13.C, E7.GND@0, E7.GND@1, J31.1, J32.1, J33.1, J34.6, J35.1, LED7.C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
- new net GND7: B8.-, C15.2, C16.2, D15.C, E8.GND@0, E8.GND@1, J36.1, J37.1, J38.1, J39.6, J40.1, LED8.C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
- new net GND8: B9.-, C17.2, C18.2, D17.C, E9.GND@0, E9.GND@1, J41.1, J42.1, J43.1, J44.6, J45.1, LED9.C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
- new net GND9: B10.-, C19.2, C20.2, D19.C, E10.GND@0, E10.GND@1, J46.1, J47.1, J48.1, J49.6, J50.1, LED10.C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
- new net GPS_RF10: E11.SIG, FB11.1, U11.11
- new net GPS_RF11: E12.SIG, FB12.1, U12.11
- new net GPS_RF12: E13.SIG, FB13.1, U13.11
- new net GPS_RF13: E14.SIG, FB14.1, U14.11
- new net GPS_RF14: E15.SIG, FB15.1, U15.11
- new net GPS_RF15: E16.SIG, FB16.1, U16.11
- new net GPS_RF6: E7.SIG, FB7.1, U7.11
- new net GPS_RF7: E8.SIG, FB8.1, U8.11
- new net GPS_RF8: E9.SIG, FB9.1, U9.11
- new net GPS_RF9: E10.SIG, FB10.1, U10.11
- new net INT10: J55.7, R151.2
- new net INT11: J60.7, R165.2
- new net INT12: J65.7, R179.2
- new net INT13: J70.7, R193.2
- new net INT14: J75.7, R207.2
- new net INT15: J80.7, R221.2
- new net INT6: J35.7, R95.2
- new net INT7: J40.7, R109.2
- new net INT8: J45.7, R123.2
- new net INT9: J50.7, R137.2
- new net N$100: PPS_LED12.1, R174.2
- new net N$101: D26.C, R173.2
- new net N$102: LED13.A, R177.1
- new net N$103: PWR12.1, R177.2
- new net N$104: J64.4, MEAS12.1, MEAS12.3
- new net N$105: JP14.1, R186.2
- new net N$106: JP14.3, R185.2
- new net N$107: D27.A, R188.1
- new net N$108: PPS_LED13.1, R188.2
- new net N$109: D28.C, R187.2
- new net N$110: LED14.A, R191.1
- new net N$111: PWR13.1, R191.2
- new net N$112: J69.4, MEAS13.1, MEAS13.3
- new net N$113: JP15.1, R200.2
- new net N$114: JP15.3, R199.2
- new net N$115: D29.A, R202.1
- new net N$116: PPS_LED14.1, R202.2
- new net N$117: D30.C, R201.2
- new net N$118: LED15.A, R205.1
- new net N$119: PWR14.1, R205.2
- new net N$120: J74.4, MEAS14.1, MEAS14.3
- new net N$121: JP16.1, R214.2
- new net N$122: JP16.3, R213.2
- new net N$123: D31.A, R216.1
- new net N$124: PPS_LED15.1, R216.2
- new net N$125: D32.C, R215.2
- new net N$126: LED16.A, R219.1
- new net N$127: PWR15.1, R219.2
- new net N$128: J79.4, MEAS15.1, MEAS15.3
- new net N$49: JP7.1, R88.2
- new net N$50: JP7.3, R87.2
- new net N$51: D13.A, R90.1
- new net N$52: PPS_LED6.1, R90.2
- new net N$53: D14.C, R89.2
- new net N$54: LED7.A, R93.1
- new net N$55: PWR6.1, R93.2
- new net N$56: J34.4, MEAS6.1, MEAS6.3
- new net N$57: JP8.1, R102.2
- new net N$58: JP8.3, R101.2
- new net N$59: D15.A, R104.1
- new net N$60: PPS_LED7.1, R104.2
- new net N$61: D16.C, R103.2
- new net N$62: LED8.A, R107.1
- new net N$63: PWR7.1, R107.2
- new net N$64: J39.4, MEAS7.1, MEAS7.3
- new net N$65: JP9.1, R116.2
- new net N$66: JP9.3, R115.2
- new net N$67: D17.A, R118.1
- new net N$68: PPS_LED8.1, R118.2
- new net N$69: D18.C, R117.2
- new net N$70: LED9.A, R121.1
- new net N$71: PWR8.1, R121.2
- new net N$72: J44.4, MEAS8.1, MEAS8.3
- new net N$73: JP10.1, R130.2
- new net N$74: JP10.3, R129.2
- new net N$75: D19.A, R132.1
- new net N$76: PPS_LED9.1, R132.2
- new net N$77: D20.C, R131.2
- new net N$78: LED10.A, R135.1
- new net N$79: PWR9.1, R135.2
- new net N$80: J49.4, MEAS9.1, MEAS9.3
- new net N$81: JP11.1, R144.2
- new net N$82: JP11.3, R143.2
- new net N$83: D21.A, R146.1
- new net N$84: PPS_LED10.1, R146.2
- new net N$85: D22.C, R145.2
- new net N$86: LED11.A, R149.1
- new net N$87: PWR10.1, R149.2
- new net N$88: J54.4, MEAS10.1, MEAS10.3
- new net N$89: JP12.1, R158.2
- new net N$90: JP12.3, R157.2
- new net N$91: D23.A, R160.1
- new net N$92: PPS_LED11.1, R160.2
- new net N$93: D24.C, R159.2
- new net N$94: LED12.A, R163.1
- new net N$95: PWR11.1, R163.2
- new net N$96: J59.4, MEAS11.1, MEAS11.3
- new net N$97: JP13.1, R172.2
- new net N$98: JP13.3, R171.2
- new net N$99: D25.A, R174.1
- new net PPS10: J55.6, PPS_LED10.2, R154.2
- new net PPS11: J60.6, PPS_LED11.2, R168.2
- new net PPS12: J65.6, PPS_LED12.2, R182.2
- new net PPS13: J70.6, PPS_LED13.2, R196.2
- new net PPS14: J75.6, PPS_LED14.2, R210.2
- new net PPS15: J80.6, PPS_LED15.2, R224.2
- new net PPS6: J35.6, PPS_LED6.2, R98.2
- new net PPS7: J40.6, PPS_LED7.2, R112.2
- new net PPS8: J45.6, PPS_LED8.2, R126.2
- new net PPS9: J50.6, PPS_LED9.2, R140.2
- new net PPS_LV10: R154.1, U11.4
- new net PPS_LV11: R168.1, U12.4
- new net PPS_LV12: R182.1, U13.4
- new net PPS_LV13: R196.1, U14.4
- new net PPS_LV14: R210.1, U15.4
- new net PPS_LV15: R224.1, U16.4
- new net PPS_LV6: R98.1, U7.4
- new net PPS_LV7: R112.1, U8.4
- new net PPS_LV8: R126.1, U9.4
- new net PPS_LV9: R140.1, U10.4
- new net RST_LV10: R152.1, U11.9
- new net RST_LV11: R166.1, U12.9
- new net RST_LV12: R180.1, U13.9
- new net RST_LV13: R194.1, U14.9
- new net RST_LV14: R208.1, U15.9
- new net RST_LV15: R222.1, U16.9
- new net RST_LV6: R96.1, U7.9
- new net RST_LV7: R110.1, U8.9
- new net RST_LV8: R124.1, U9.9
- new net RST_LV9: R138.1, U10.9
- new net RXI10: J54.3, J55.5, R142.2
- new net RXI11: J59.3, J60.5, R156.2
- new net RXI12: J64.3, J65.5, R170.2
- new net RXI13: J69.3, J70.5, R184.2
- new net RXI14: J74.3, J75.5, R198.2
- new net RXI15: J79.3, J80.5, R212.2
- new net RXI6: J34.3, J35.5, R86.2
- new net RXI7: J39.3, J40.5, R100.2
- new net RXI8: J44.3, J45.5, R114.2
- new net RXI9: J49.3, J50.5, R128.2
- new net RXLV10: R142.1, U11.3
- new net RXLV11: R156.1, U12.3
- new net RXLV12: R170.1, U13.3
- new net RXLV13: R184.1, U14.3
- new net RXLV14: R198.1, U15.3
- new net RXLV15: R212.1, U16.3
- new net RXLV6: R86.1, U7.3
- new net RXLV7: R100.1, U8.3
- new net RXLV8: R114.1, U9.3
- new net RXLV9: R128.1, U10.3
- new net SAFE_LV10: R153.1, U11.18
- new net SAFE_LV11: R167.1, U12.18
- new net SAFE_LV12: R181.1, U13.18
- new net SAFE_LV13: R195.1, U14.18
- new net SAFE_LV14: R209.1, U15.18
- new net SAFE_LV15: R223.1, U16.18
- new net SAFE_LV6: R97.1, U7.18
- new net SAFE_LV7: R111.1, U8.18
- new net SAFE_LV8: R125.1, U9.18
- new net SAFE_LV9: R139.1, U10.18
- new net SCL10: J51.4, J52.4, J53.4, R143.1, R148.2
- new net SCL11: J56.4, J57.4, J58.4, R157.1, R162.2
- new net SCL12: J61.4, J62.4, J63.4, R171.1, R176.2
- new net SCL13: J66.4, J67.4, J68.4, R185.1, R190.2
- new net SCL14: J71.4, J72.4, J73.4, R199.1, R204.2
- new net SCL15: J76.4, J77.4, J78.4, R213.1, R218.2
- new net SCL6: J31.4, J32.4, J33.4, R87.1, R92.2
- new net SCL7: J36.4, J37.4, J38.4, R101.1, R106.2
- new net SCL8: J41.4, J42.4, J43.4, R115.1, R120.2
- new net SCL9: J46.4, J47.4, J48.4, R129.1, R134.2
- new net SCL_LV10: R148.1, U11.17
- new net SCL_LV11: R162.1, U12.17
- new net SCL_LV12: R176.1, U13.17
- new net SCL_LV13: R190.1, U14.17
- new net SCL_LV14: R204.1, U15.17
- new net SCL_LV15: R218.1, U16.17
- new net SCL_LV6: R92.1, U7.17
- new net SCL_LV7: R106.1, U8.17
- new net SCL_LV8: R120.1, U9.17
- new net SCL_LV9: R134.1, U10.17
- new net SDA10: J51.3, J52.3, J53.3, R144.1, R147.2
- new net SDA11: J56.3, J57.3, J58.3, R158.1, R161.2
- new net SDA12: J61.3, J62.3, J63.3, R172.1, R175.2
- new net SDA13: J66.3, J67.3, J68.3, R186.1, R189.2
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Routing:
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- added copper zone on layer 1, net GND10
- added copper zone on layer 16, net GND10
- added copper zone on layer 1, net GND11
- added copper zone on layer 16, net GND11
- added copper zone on layer 1, net GND12
- added copper zone on layer 16, net GND12
- added copper zone on layer 1, net GND13
- added copper zone on layer 16, net GND13
- added copper zone on layer 1, net GND14
- added copper zone on layer 16, net GND14
- added copper zone on layer 1, net GND15
- added copper zone on layer 16, net GND15
- added copper zone on layer 1, net GND6
- added copper zone on layer 16, net GND6
- added copper zone on layer 1, net GND7
- added copper zone on layer 16, net GND7
- added copper zone on layer 1, net GND8
- added copper zone on layer 16, net GND8
- added copper zone on layer 1, net GND9
- added copper zone on layer 16, net GND9
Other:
- board size 114.3 x 106.2 mm -> 203.2 x 137.2 mm
